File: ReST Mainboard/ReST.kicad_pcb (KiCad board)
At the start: 2 copper layers, 100 x 100 mm, 95 parts, among them IC1 AT24C128, P1 CONN_02X08, P10 CONN_01X04, P11 CONN_01X04, P12 CONN_02X04, P13 CONN_01X03, P14 CONN_02X03, P15 CONN_01X05, P16 CONN_01X03, P17 CONN_01X04, P18 CONN_02X04, P19 CONN_01X04, P2 CONN_02X08, P20 CONN_02X04, P21 CONN_02X04, P22 CONN_01X03, P23 CONN_01X06, P24 CONN_01X03, P25 CONN_01X06, P26 CONN_01X03, P27 CONN_01X06, P28 CONN_01X03, P3 CONN_02X07, P30 CONN_01X03, P32 CONN_01X03, P34 CONN_01X03, P35 SCREW_01X04, P36 SCREW_01X04, P37 SCREW_01X04, P38 SCREW_01X04, P39 CONN_02X04, P4 CONN_02X10, P40 CONN_01X04, P41 CONN_01X04, P42 CONN_01X04, P43 CONN_02X03, P44 CONN_02X03, P45 CONN_02X03, P46 CONN_02X03, P5 USB_OTG, P6 CONN_02X05, P7 CONN_02X05, P8 CONN_01X09, P9 CONN_01X02, SW1 SW-SPST-NO, U1 STM32F103VE, U2 USBLC6-2, U3 L7805ACD2T-TR, U4 LM2574N-ADJ, U5 POLOLU_A4988, U6 POLOLU_A4988, U7 POLOLU_A4988, U8 POLOLU_A4988, X1 Crystal_Small

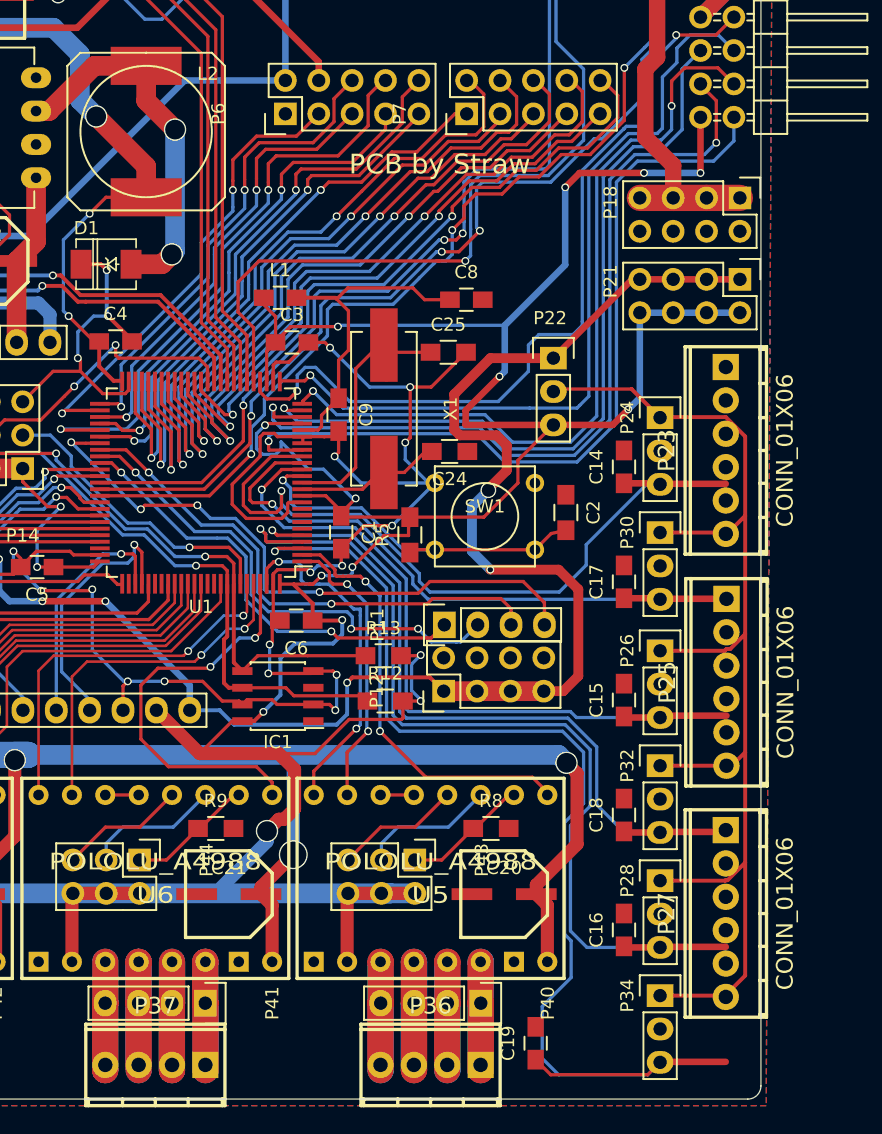
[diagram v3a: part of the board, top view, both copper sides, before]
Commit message: Added relative paths and linked footprint to a extra repo
hope i finally fixed the problem with missing libs. will try to add the
3d views, too
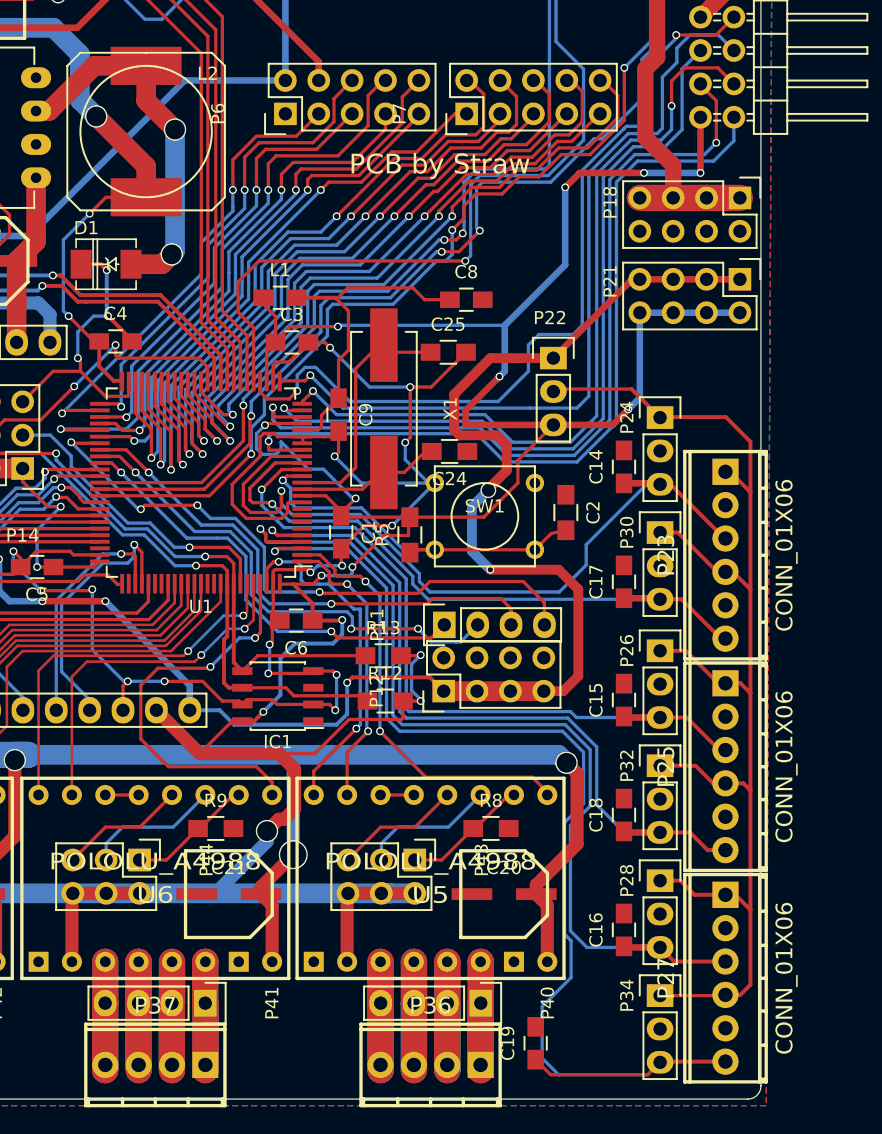
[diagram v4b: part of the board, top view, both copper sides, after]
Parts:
- moved P23 7.98 mm to (196.8, 114.0)
- moved P25 6.43 mm to (196.8, 130.2)
- moved P27 4.93 mm to (196.8, 146.2)
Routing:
- net /ENDSTOP_VCC: track 38.9 -> 100.1 mm
- net /X-MAX: track 78.5 -> 49.5 mm
- net /Y-MAX: track 78.7 -> 58.2 mm
- net /Z-MAX: track 90.8 -> 88.7 mm
- net /X-MIN: track 56.6 -> 58.4 mm
- net /Y-MIN: track 55.7 -> 56.8 mm

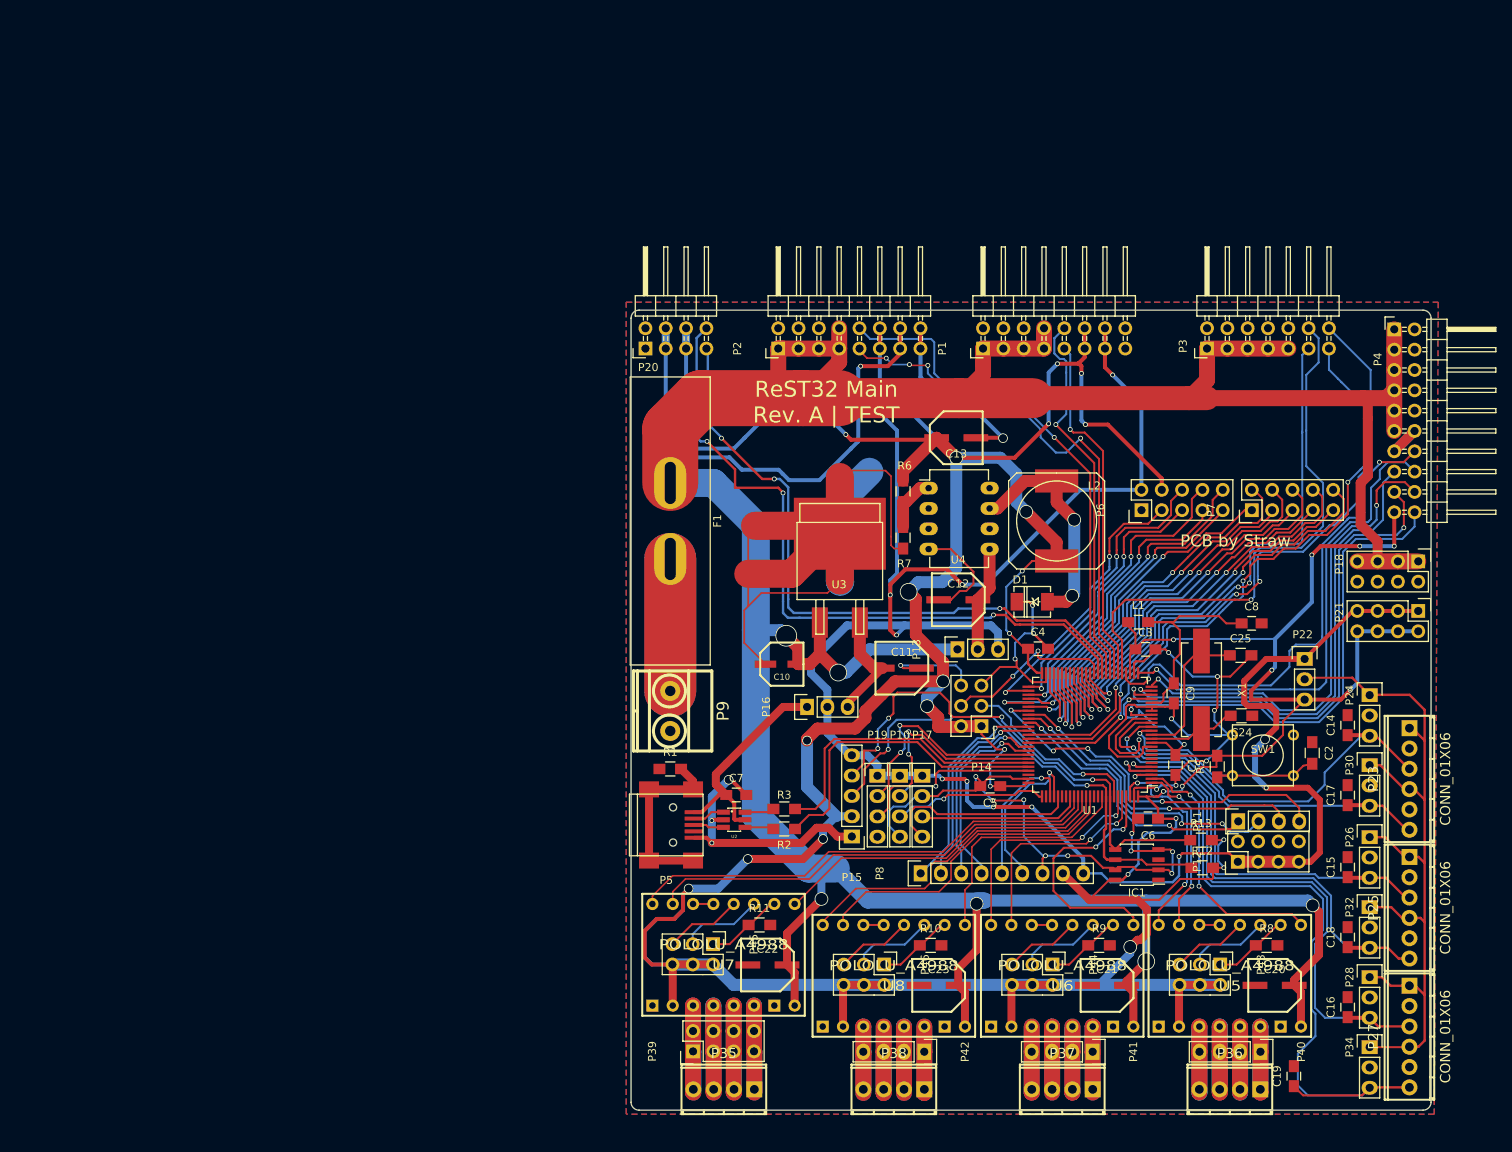
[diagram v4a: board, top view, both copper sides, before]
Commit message: Finished PCB design, notations and silkscreen
gonna work to finish a combined design for cheaper pcb cost and put
everything i need into the bom
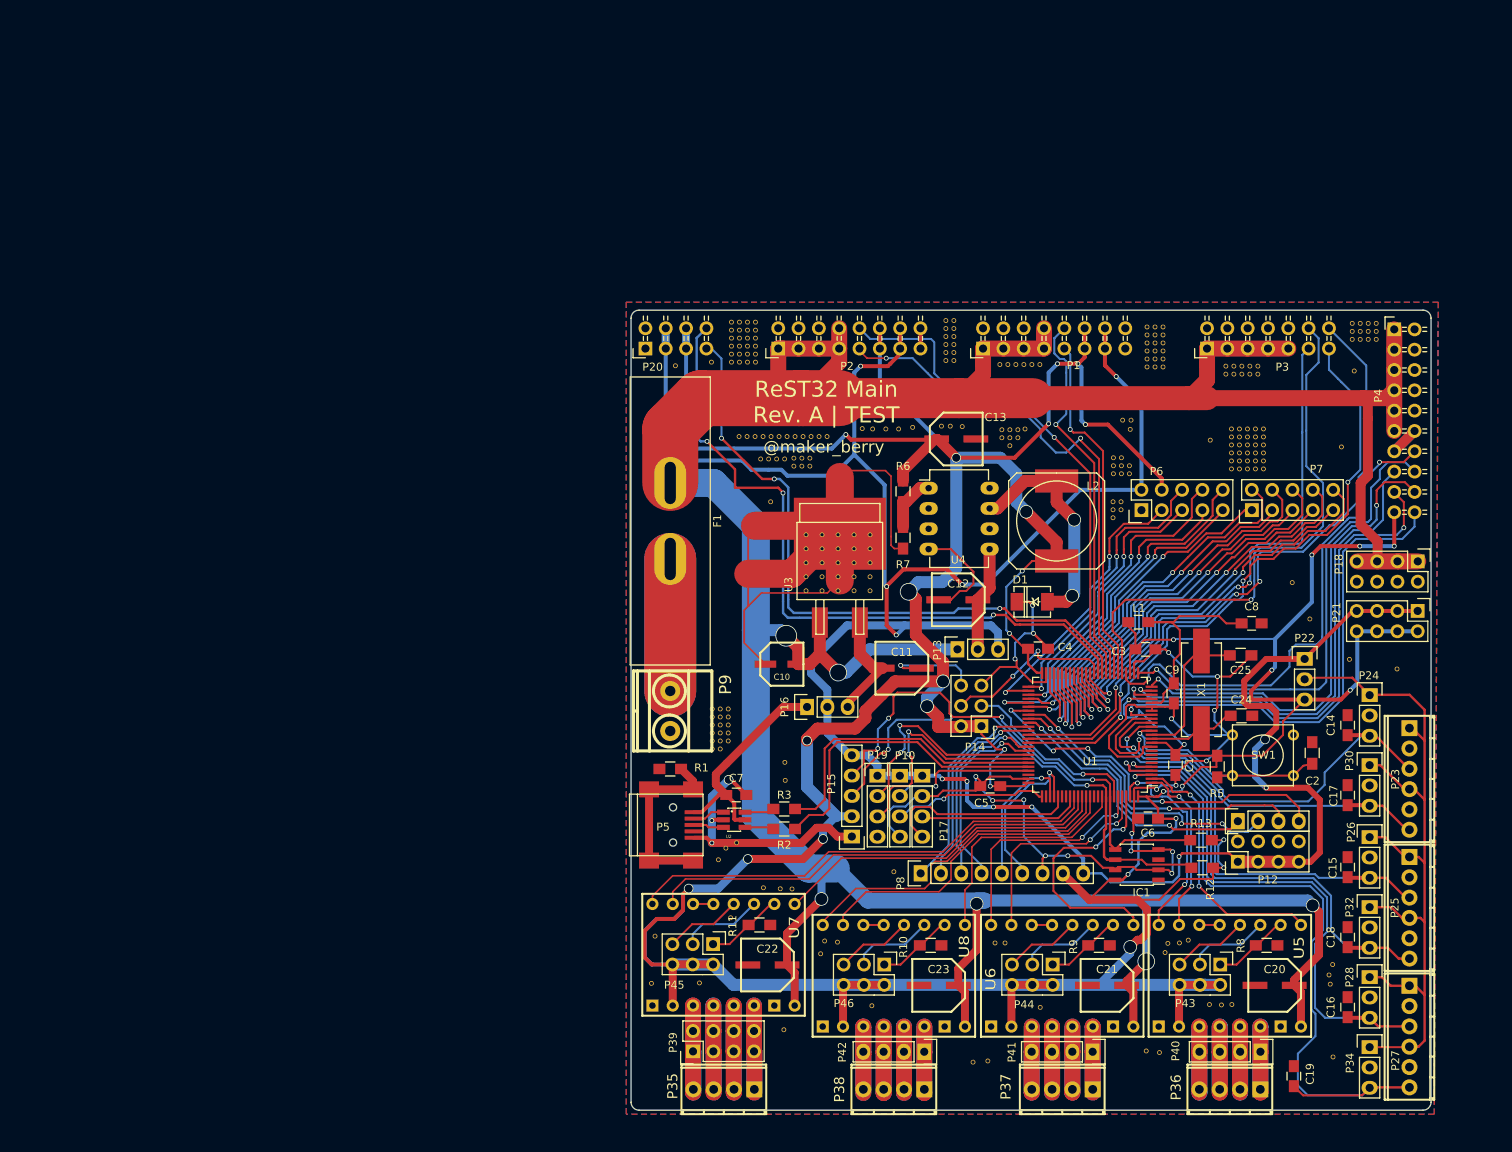
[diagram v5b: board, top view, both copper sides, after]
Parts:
- added REF**11: VIA-0.6mm, ReST-Library:VIA-0.6mm, F.Cu at (119.8, 74.0)
- added REF**111: VIA-0.6mm, ReST-Library:VIA-0.6mm, F.Cu at (115.7, 74.0)
- added REF**111: VIA-0.6mm, ReST-Library:VIA-0.6mm, F.Cu at (109.6, 105.3)
- added REF**111: VIA-0.6mm, ReST-Library:VIA-0.6mm, F.Cu at (112.0, 57.0)
- added REF**11101: VIA-0.6mm, ReST-Library:VIA-0.6mm, F.Cu at (122.0, 71.2)
- added REF**1111: VIA-0.6mm, ReST-Library:VIA-0.6mm, F.Cu at (113.0, 71.2)
- added REF**1111: VIA-0.6mm, ReST-Library:VIA-0.6mm, F.Cu at (163.9, 57.5)
- added REF**11111: VIA-0.6mm, ReST-Library:VIA-0.6mm, F.Cu at (123.0, 71.2)
- added REF**11111: VIA-0.6mm, ReST-Library:VIA-0.6mm, F.Cu at (138.8, 56.8)
- added REF**111111: VIA-0.6mm, ReST-Library:VIA-0.6mm, F.Cu at (174.5, 70.3)
- added REF**111112: VIA-0.6mm, ReST-Library:VIA-0.6mm, F.Cu at (174.5, 71.3)
- added REF**111113: VIA-0.6mm, ReST-Library:VIA-0.6mm, F.Cu at (174.5, 72.3)
- added REF**111114: VIA-0.6mm, ReST-Library:VIA-0.6mm, F.Cu at (174.5, 73.3)
- added REF**111115: VIA-0.6mm, ReST-Library:VIA-0.6mm, F.Cu at (174.5, 74.3)
- added REF**111116: VIA-0.6mm, ReST-Library:VIA-0.6mm, F.Cu at (174.5, 75.3)
- added REF**11112: VIA-0.6mm, ReST-Library:VIA-0.6mm, F.Cu at (138.8, 57.8)
- added REF**111121: VIA-0.6mm, ReST-Library:VIA-0.6mm, F.Cu at (175.5, 70.3)
- added REF**111122: VIA-0.6mm, ReST-Library:VIA-0.6mm, F.Cu at (175.5, 71.3)
- added REF**111123: VIA-0.6mm, ReST-Library:VIA-0.6mm, F.Cu at (175.5, 72.3)
- added REF**111124: VIA-0.6mm, ReST-Library:VIA-0.6mm, F.Cu at (175.5, 73.3)
- added REF**111125: VIA-0.6mm, ReST-Library:VIA-0.6mm, F.Cu at (175.5, 74.3)
- added REF**111126: VIA-0.6mm, ReST-Library:VIA-0.6mm, F.Cu at (175.5, 75.3)
- added REF**11113: VIA-0.6mm, ReST-Library:VIA-0.6mm, F.Cu at (138.8, 58.8)
- added REF**111131: VIA-0.6mm, ReST-Library:VIA-0.6mm, F.Cu at (176.5, 70.3)
- added REF**111132: VIA-0.6mm, ReST-Library:VIA-0.6mm, F.Cu at (176.5, 71.3)
- added REF**111133: VIA-0.6mm, ReST-Library:VIA-0.6mm, F.Cu at (176.5, 72.3)
- added REF**111134: VIA-0.6mm, ReST-Library:VIA-0.6mm, F.Cu at (176.5, 73.3)
- added REF**111135: VIA-0.6mm, ReST-Library:VIA-0.6mm, F.Cu at (176.5, 74.3)
- added REF**111136: VIA-0.6mm, ReST-Library:VIA-0.6mm, F.Cu at (176.5, 75.3)
- added REF**11114: VIA-0.6mm, ReST-Library:VIA-0.6mm, F.Cu at (138.8, 59.8)
- added REF**111141: VIA-0.6mm, ReST-Library:VIA-0.6mm, F.Cu at (177.5, 70.3)
- added REF**111142: VIA-0.6mm, ReST-Library:VIA-0.6mm, F.Cu at (177.5, 71.3)
- added REF**111143: VIA-0.6mm, ReST-Library:VIA-0.6mm, F.Cu at (177.5, 72.3)
- added REF**111144: VIA-0.6mm, ReST-Library:VIA-0.6mm, F.Cu at (177.5, 73.3)
- added REF**111145: VIA-0.6mm, ReST-Library:VIA-0.6mm, F.Cu at (177.5, 74.3)
- added REF**111146: VIA-0.6mm, ReST-Library:VIA-0.6mm, F.Cu at (177.5, 75.3)
- added REF**11115: VIA-0.6mm, ReST-Library:VIA-0.6mm, F.Cu at (138.8, 60.8)
- added REF**111151: VIA-0.6mm, ReST-Library:VIA-0.6mm, F.Cu at (178.5, 70.3)
- added REF**111152: VIA-0.6mm, ReST-Library:VIA-0.6mm, F.Cu at (178.5, 71.3)
- added REF**111153: VIA-0.6mm, ReST-Library:VIA-0.6mm, F.Cu at (178.5, 72.3)
- added REF**111154: VIA-0.6mm, ReST-Library:VIA-0.6mm, F.Cu at (178.5, 73.3)
- added REF**111155: VIA-0.6mm, ReST-Library:VIA-0.6mm, F.Cu at (178.5, 74.3)
- added REF**111156: VIA-0.6mm, ReST-Library:VIA-0.6mm, F.Cu at (178.5, 75.3)
- added REF**11116: VIA-0.6mm, ReST-Library:VIA-0.6mm, F.Cu at (138.8, 61.8)
- added REF**1112: VIA-0.6mm, ReST-Library:VIA-0.6mm, F.Cu at (163.9, 58.5)
- added REF**11121: VIA-0.6mm, ReST-Library:VIA-0.6mm, F.Cu at (124.0, 71.2)
- added REF**11121: VIA-0.6mm, ReST-Library:VIA-0.6mm, F.Cu at (139.8, 56.8)
- added REF**11122: VIA-0.6mm, ReST-Library:VIA-0.6mm, F.Cu at (139.8, 57.8)
- added REF**11123: VIA-0.6mm, ReST-Library:VIA-0.6mm, F.Cu at (139.8, 58.8)
- added REF**11124: VIA-0.6mm, ReST-Library:VIA-0.6mm, F.Cu at (139.8, 59.8)
- added REF**11125: VIA-0.6mm, ReST-Library:VIA-0.6mm, F.Cu at (139.8, 60.8)
- added REF**11126: VIA-0.6mm, ReST-Library:VIA-0.6mm, F.Cu at (139.8, 61.8)
- added REF**1113: VIA-0.6mm, ReST-Library:VIA-0.6mm, F.Cu at (163.9, 59.5)
- added REF**1114: VIA-0.6mm, ReST-Library:VIA-0.6mm, F.Cu at (163.9, 60.5)
- added REF**1115: VIA-0.6mm, ReST-Library:VIA-0.6mm, F.Cu at (163.9, 61.5)
- added REF**1116: VIA-0.6mm, ReST-Library:VIA-0.6mm, F.Cu at (163.9, 62.5)
- added REF**112: VIA-0.6mm, ReST-Library:VIA-0.6mm, F.Cu at (109.6, 106.3)
- added REF**112: VIA-0.6mm, ReST-Library:VIA-0.6mm, F.Cu at (112.0, 58.0)
- added REF**1121: VIA-0.6mm, ReST-Library:VIA-0.6mm, F.Cu at (114.0, 71.2)
- added REF**1121: VIA-0.6mm, ReST-Library:VIA-0.6mm, F.Cu at (164.9, 57.5)
- added REF**1122: VIA-0.6mm, ReST-Library:VIA-0.6mm, F.Cu at (164.9, 58.5)
- added REF**1123: VIA-0.6mm, ReST-Library:VIA-0.6mm, F.Cu at (164.9, 59.5)
- added REF**1124: VIA-0.6mm, ReST-Library:VIA-0.6mm, F.Cu at (164.9, 60.5)
- added REF**1125: VIA-0.6mm, ReST-Library:VIA-0.6mm, F.Cu at (164.9, 61.5)
- added REF**1126: VIA-0.6mm, ReST-Library:VIA-0.6mm, F.Cu at (164.9, 62.5)
- added REF**113: VIA-0.6mm, ReST-Library:VIA-0.6mm, F.Cu at (109.6, 107.3)
- added REF**113: VIA-0.6mm, ReST-Library:VIA-0.6mm, F.Cu at (112.0, 59.0)
- added REF**1131: VIA-0.6mm, ReST-Library:VIA-0.6mm, F.Cu at (115.0, 71.2)
- added REF**1131: VIA-0.6mm, ReST-Library:VIA-0.6mm, F.Cu at (165.9, 57.5)
- added REF**1132: VIA-0.6mm, ReST-Library:VIA-0.6mm, F.Cu at (165.9, 58.5)
- added REF**1133: VIA-0.6mm, ReST-Library:VIA-0.6mm, F.Cu at (165.9, 59.5)
- added REF**1134: VIA-0.6mm, ReST-Library:VIA-0.6mm, F.Cu at (165.9, 60.5)
- added REF**1135: VIA-0.6mm, ReST-Library:VIA-0.6mm, F.Cu at (165.9, 61.5)
- added REF**1136: VIA-0.6mm, ReST-Library:VIA-0.6mm, F.Cu at (165.9, 62.5)
- added REF**114: VIA-0.6mm, ReST-Library:VIA-0.6mm, F.Cu at (109.6, 108.3)
- added REF**114: VIA-0.6mm, ReST-Library:VIA-0.6mm, F.Cu at (112.0, 60.0)
- added REF**1141: VIA-0.6mm, ReST-Library:VIA-0.6mm, F.Cu at (116.0, 71.2)
- added REF**115: VIA-0.6mm, ReST-Library:VIA-0.6mm, F.Cu at (109.6, 109.3)
- added REF**115: VIA-0.6mm, ReST-Library:VIA-0.6mm, F.Cu at (112.0, 61.0)
- added REF**1151: VIA-0.6mm, ReST-Library:VIA-0.6mm, F.Cu at (117.0, 71.2)
- added REF**116: VIA-0.6mm, ReST-Library:VIA-0.6mm, F.Cu at (109.6, 110.3)
- added REF**116: VIA-0.6mm, ReST-Library:VIA-0.6mm, F.Cu at (112.0, 62.0)
- added REF**1161: VIA-0.6mm, ReST-Library:VIA-0.6mm, F.Cu at (118.0, 71.2)
- added REF**1171: VIA-0.6mm, ReST-Library:VIA-0.6mm, F.Cu at (119.0, 71.2)
- added REF**1181: VIA-0.6mm, ReST-Library:VIA-0.6mm, F.Cu at (120.0, 71.2)
- added REF**1191: VIA-0.6mm, ReST-Library:VIA-0.6mm, F.Cu at (121.0, 71.2)
- added REF**12: VIA-0.6mm, ReST-Library:VIA-0.6mm, F.Cu at (119.8, 75.0)
- added REF**121: VIA-0.6mm, ReST-Library:VIA-0.6mm, F.Cu at (116.7, 74.0)
- added REF**121: VIA-0.6mm, ReST-Library:VIA-0.6mm, F.Cu at (110.6, 105.3)
- added REF**121: VIA-0.6mm, ReST-Library:VIA-0.6mm, F.Cu at (113.0, 57.0)
- added REF**122: VIA-0.6mm, ReST-Library:VIA-0.6mm, F.Cu at (110.6, 106.3)
- added REF**122: VIA-0.6mm, ReST-Library:VIA-0.6mm, F.Cu at (113.0, 58.0)
- added REF**123: VIA-0.6mm, ReST-Library:VIA-0.6mm, F.Cu at (110.6, 107.3)
- added REF**123: VIA-0.6mm, ReST-Library:VIA-0.6mm, F.Cu at (113.0, 59.0)
- added REF**124: VIA-0.6mm, ReST-Library:VIA-0.6mm, F.Cu at (110.6, 108.3)
- added REF**124: VIA-0.6mm, ReST-Library:VIA-0.6mm, F.Cu at (113.0, 60.0)
- added REF**125: VIA-0.6mm, ReST-Library:VIA-0.6mm, F.Cu at (110.6, 109.3)
- added REF**125: VIA-0.6mm, ReST-Library:VIA-0.6mm, F.Cu at (113.0, 61.0)
- added REF**126: VIA-0.6mm, ReST-Library:VIA-0.6mm, F.Cu at (110.6, 110.3)
- added REF**126: VIA-0.6mm, ReST-Library:VIA-0.6mm, F.Cu at (113.0, 62.0)
- added REF**131: VIA-0.6mm, ReST-Library:VIA-0.6mm, F.Cu at (118.7, 114.2)
- added REF**131: VIA-0.6mm, ReST-Library:VIA-0.6mm, F.Cu at (118.7, 112.0)
- added REF**131: VIA-0.6mm, ReST-Library:VIA-0.6mm, F.Cu at (117.7, 74.0)
- added REF**131: VIA-0.6mm, ReST-Library:VIA-0.6mm, F.Cu at (111.6, 105.3)
- added REF**131: VIA-0.6mm, ReST-Library:VIA-0.6mm, F.Cu at (114.0, 57.0)
- added REF**131111: VIA-0.6mm, ReST-Library:VIA-0.6mm, F.Cu at (121.3, 83.5)
- added REF**131112: VIA-0.6mm, ReST-Library:VIA-0.6mm, F.Cu at (121.3, 85.3)
- added REF**131113: VIA-0.6mm, ReST-Library:VIA-0.6mm, F.Cu at (121.3, 87.0)
- added REF**131114: VIA-0.6mm, ReST-Library:VIA-0.6mm, F.Cu at (121.3, 88.8)
- added REF**131115: VIA-0.6mm, ReST-Library:VIA-0.6mm, F.Cu at (121.3, 90.5)
- added REF**131121: VIA-0.6mm, ReST-Library:VIA-0.6mm, F.Cu at (123.3, 83.5)
- added REF**131122: VIA-0.6mm, ReST-Library:VIA-0.6mm, F.Cu at (123.3, 85.3)
- added REF**131123: VIA-0.6mm, ReST-Library:VIA-0.6mm, F.Cu at (123.3, 87.0)
- added REF**131124: VIA-0.6mm, ReST-Library:VIA-0.6mm, F.Cu at (123.3, 88.8)
- added REF**131125: VIA-0.6mm, ReST-Library:VIA-0.6mm, F.Cu at (123.3, 90.5)
- added REF**131131: VIA-0.6mm, ReST-Library:VIA-0.6mm, F.Cu at (125.3, 83.5)
- added REF**131132: VIA-0.6mm, ReST-Library:VIA-0.6mm, F.Cu at (125.3, 85.3)
- added REF**131133: VIA-0.6mm, ReST-Library:VIA-0.6mm, F.Cu at (125.3, 87.0)
- added REF**131134: VIA-0.6mm, ReST-Library:VIA-0.6mm, F.Cu at (125.3, 88.8)
- added REF**131135: VIA-0.6mm, ReST-Library:VIA-0.6mm, F.Cu at (125.3, 90.5)
- added REF**131141: VIA-0.6mm, ReST-Library:VIA-0.6mm, F.Cu at (127.3, 83.5)
- added REF**131142: VIA-0.6mm, ReST-Library:VIA-0.6mm, F.Cu at (127.3, 85.3)
- added REF**131143: VIA-0.6mm, ReST-Library:VIA-0.6mm, F.Cu at (127.3, 87.0)
- added REF**131144: VIA-0.6mm, ReST-Library:VIA-0.6mm, F.Cu at (127.3, 88.8)
- added REF**131145: VIA-0.6mm, ReST-Library:VIA-0.6mm, F.Cu at (127.3, 90.5)
- added REF**131151: VIA-0.6mm, ReST-Library:VIA-0.6mm, F.Cu at (129.3, 83.5)
- added REF**131152: VIA-0.6mm, ReST-Library:VIA-0.6mm, F.Cu at (129.3, 85.3)
- added REF**131153: VIA-0.6mm, ReST-Library:VIA-0.6mm, F.Cu at (129.3, 87.0)
- added REF**131154: VIA-0.6mm, ReST-Library:VIA-0.6mm, F.Cu at (129.3, 88.8)
- added REF**131155: VIA-0.6mm, ReST-Library:VIA-0.6mm, F.Cu at (129.3, 90.5)
- added REF**132: VIA-0.6mm, ReST-Library:VIA-0.6mm, F.Cu at (111.6, 106.3)
- added REF**132: VIA-0.6mm, ReST-Library:VIA-0.6mm, F.Cu at (114.0, 58.0)
- added REF**133: VIA-0.6mm, ReST-Library:VIA-0.6mm, F.Cu at (111.6, 107.3)
- added REF**133: VIA-0.6mm, ReST-Library:VIA-0.6mm, F.Cu at (114.0, 59.0)
- added REF**134: VIA-0.6mm, ReST-Library:VIA-0.6mm, F.Cu at (111.6, 108.3)
- added REF**134: VIA-0.6mm, ReST-Library:VIA-0.6mm, F.Cu at (114.0, 60.0)
- added REF**135: VIA-0.6mm, ReST-Library:VIA-0.6mm, F.Cu at (111.6, 109.3)
- added REF**135: VIA-0.6mm, ReST-Library:VIA-0.6mm, F.Cu at (114.0, 61.0)
- added REF**136: VIA-0.6mm, ReST-Library:VIA-0.6mm, F.Cu at (114.0, 62.0)
- added REF**141: VIA-0.6mm, ReST-Library:VIA-0.6mm, F.Cu at (118.7, 74.0)
- added REF**141: VIA-0.6mm, ReST-Library:VIA-0.6mm, F.Cu at (115.0, 57.0)
- added REF**142: VIA-0.6mm, ReST-Library:VIA-0.6mm, F.Cu at (115.0, 58.0)
- added REF**143: VIA-0.6mm, ReST-Library:VIA-0.6mm, F.Cu at (115.0, 59.0)
- added REF**144: VIA-0.6mm, ReST-Library:VIA-0.6mm, F.Cu at (115.0, 60.0)
- added REF**145: VIA-0.6mm, ReST-Library:VIA-0.6mm, F.Cu at (115.0, 61.0)
- added REF**146: VIA-0.6mm, ReST-Library:VIA-0.6mm, F.Cu at (115.0, 62.0)
- added REF**21: VIA-0.6mm, ReST-Library:VIA-0.6mm, F.Cu at (120.8, 74.0)
- added REF**22: VIA-0.6mm, ReST-Library:VIA-0.6mm, F.Cu at (120.8, 75.0)
- added REF**31: VIA-0.6mm, ReST-Library:VIA-0.6mm, F.Cu at (110.4, 124.2)
- added REF**31: VIA-0.6mm, ReST-Library:VIA-0.6mm, F.Cu at (142.2, 149.4)
- added REF**31: VIA-0.6mm, ReST-Library:VIA-0.6mm, F.Cu at (129.6, 142.4)
- added REF**31: VIA-0.6mm, ReST-Library:VIA-0.6mm, F.Cu at (123.2, 135.9)
- added REF**31: VIA-0.6mm, ReST-Library:VIA-0.6mm, F.Cu at (125.2, 134.4)
- added REF**31: VIA-0.6mm, ReST-Library:VIA-0.6mm, F.Cu at (123.7, 134.3)
- added REF**31: VIA-0.6mm, ReST-Library:VIA-0.6mm, F.Cu at (146.2, 134.6)
- added REF**31: VIA-0.6mm, ReST-Library:VIA-0.6mm, F.Cu at (144.9, 134.6)
- added REF**31: VIA-0.6mm, ReST-Library:VIA-0.6mm, F.Cu at (150.6, 142.6)
- added REF**31: VIA-0.6mm, ReST-Library:VIA-0.6mm, F.Cu at (165.5, 148.2)
- added REF**31: VIA-0.6mm, ReST-Library:VIA-0.6mm, F.Cu at (163.8, 148.1)
- added REF**31: VIA-0.6mm, ReST-Library:VIA-0.6mm, F.Cu at (112.7, 122.0)
- added REF**31: VIA-0.6mm, ReST-Library:VIA-0.6mm, F.Cu at (187.2, 148.8)
- added REF**31: VIA-0.6mm, ReST-Library:VIA-0.6mm, F.Cu at (186.8, 139.7)
- added REF**31: VIA-0.6mm, ReST-Library:VIA-0.6mm, F.Cu at (186.7, 138.6)
- added REF**31: VIA-0.6mm, ReST-Library:VIA-0.6mm, F.Cu at (187.2, 137.2)
- added REF**31: VIA-0.6mm, ReST-Library:VIA-0.6mm, F.Cu at (174.6, 142.2)
- added REF**31: VIA-0.6mm, ReST-Library:VIA-0.6mm, F.Cu at (173.2, 142.3)
- added REF**31: VIA-0.6mm, ReST-Library:VIA-0.6mm, F.Cu at (171.8, 142.2)
- added REF**31: VIA-0.6mm, ReST-Library:VIA-0.6mm, F.Cu at (166.2, 135.8)
- added REF**31: VIA-0.6mm, ReST-Library:VIA-0.6mm, F.Cu at (169.1, 134.2)
- added REF**31: VIA-0.6mm, ReST-Library:VIA-0.6mm, F.Cu at (168.0, 134.6)
- added REF**31: VIA-0.6mm, ReST-Library:VIA-0.6mm, F.Cu at (111.3, 122.7)
- added REF**31: VIA-0.6mm, ReST-Library:VIA-0.6mm, F.Cu at (161.8, 70.3)
- added REF**31: VIA-0.6mm, ReST-Library:VIA-0.6mm, F.Cu at (161.9, 69.2)
- added REF**31: VIA-0.6mm, ReST-Library:VIA-0.6mm, F.Cu at (160.9, 69.2)
- added REF**31: VIA-0.6mm, ReST-Library:VIA-0.6mm, F.Cu at (102.5, 133.7)
- added REF**31: VIA-0.6mm, ReST-Library:VIA-0.6mm, F.Cu at (111.9, 131.4)
- added REF**31: VIA-0.6mm, ReST-Library:VIA-0.6mm, F.Cu at (112.0, 133.3)
- added REF**31: VIA-0.6mm, ReST-Library:VIA-0.6mm, F.Cu at (116.0, 127.7)
- added REF**31: VIA-0.6mm, ReST-Library:VIA-0.6mm, F.Cu at (132.3, 125.7)
- added REF**31: VIA-0.6mm, ReST-Library:VIA-0.6mm, F.Cu at (166.6, 134.6)
- added REF**31: VIA-0.6mm, ReST-Library:VIA-0.6mm, F.Cu at (189.2, 99.1)
- added REF**31: VIA-0.6mm, ReST-Library:VIA-0.6mm, F.Cu at (119.6, 127.8)
- added REF**31: VIA-0.6mm, ReST-Library:VIA-0.6mm, F.Cu at (195.2, 100.3)
- added REF**31: VIA-0.6mm, ReST-Library:VIA-0.6mm, F.Cu at (184.3, 94.0)
- added REF**31: VIA-0.6mm, ReST-Library:VIA-0.6mm, F.Cu at (182.1, 89.5)
- added REF**31: VIA-0.6mm, ReST-Library:VIA-0.6mm, F.Cu at (189.8, 63.0)
- added REF**31: VIA-0.6mm, ReST-Library:VIA-0.6mm, F.Cu at (188.2, 72.5)
- added REF**31: VIA-0.6mm, ReST-Library:VIA-0.6mm, F.Cu at (171.8, 71.7)
- added REF**31: VIA-0.6mm, ReST-Library:VIA-0.6mm, F.Cu at (109.5, 62.0)
- added REF**31: VIA-0.6mm, ReST-Library:VIA-0.6mm, F.Cu at (105.0, 62.4)
- added REF**31: VIA-0.6mm, ReST-Library:VIA-0.6mm, F.Cu at (116.9, 79.4)
- added REF**31: VIA-0.6mm, ReST-Library:VIA-0.6mm, F.Cu at (121.8, 74.0)
- added REF**31: VIA-0.6mm, ReST-Library:VIA-0.6mm, F.Cu at (118.1, 127.8)
- added REF**31: VIA-0.6mm, ReST-Library:VIA-0.6mm, F.Cu at (102.0, 139.6)
- added REF**31: VIA-0.6mm, ReST-Library:VIA-0.6mm, F.Cu at (108.0, 139.6)
- added REF**31: VIA-0.6mm, ReST-Library:VIA-0.6mm, F.Cu at (118.5, 145.4)
- added REF**31: VIA-0.6mm, ReST-Library:VIA-0.6mm, F.Cu at (144.1, 149.3)
- added REF**311: VIA-0.6mm, ReST-Library:VIA-0.6mm, F.Cu at (145.8, 70.4)
- added REF**311: VIA-0.6mm, ReST-Library:VIA-0.6mm, F.Cu at (189.6, 57.1)
- added REF**311: VIA-0.6mm, ReST-Library:VIA-0.6mm, F.Cu at (159.8, 73.9)
- added REF**3111: VIA-0.6mm, ReST-Library:VIA-0.6mm, F.Cu at (173.8, 62.5)
- added REF**3111: VIA-0.6mm, ReST-Library:VIA-0.6mm, F.Cu at (159.7, 79.4)
- added REF**3111: VIA-0.6mm, ReST-Library:VIA-0.6mm, F.Cu at (145.6, 62.2)
- added REF**3112: VIA-0.6mm, ReST-Library:VIA-0.6mm, F.Cu at (173.8, 63.5)
- added REF**3112: VIA-0.6mm, ReST-Library:VIA-0.6mm, F.Cu at (159.7, 80.4)
- added REF**3113: VIA-0.6mm, ReST-Library:VIA-0.6mm, F.Cu at (159.7, 81.4)
- added REF**312: VIA-0.6mm, ReST-Library:VIA-0.6mm, F.Cu at (145.8, 71.4)
- added REF**312: VIA-0.6mm, ReST-Library:VIA-0.6mm, F.Cu at (189.6, 58.1)
- added REF**312: VIA-0.6mm, ReST-Library:VIA-0.6mm, F.Cu at (159.8, 74.9)
- added REF**3121: VIA-0.6mm, ReST-Library:VIA-0.6mm, F.Cu at (174.8, 62.5)
- added REF**3121: VIA-0.6mm, ReST-Library:VIA-0.6mm, F.Cu at (160.7, 79.4)
- added REF**3121: VIA-0.6mm, ReST-Library:VIA-0.6mm, F.Cu at (146.6, 62.2)
- added REF**3122: VIA-0.6mm, ReST-Library:VIA-0.6mm, F.Cu at (174.8, 63.5)
- added REF**3122: VIA-0.6mm, ReST-Library:VIA-0.6mm, F.Cu at (160.7, 80.4)
- added REF**313: VIA-0.6mm, ReST-Library:VIA-0.6mm, F.Cu at (128.3, 70.2)
- added REF**313: VIA-0.6mm, ReST-Library:VIA-0.6mm, F.Cu at (159.8, 75.9)
- added REF**313: VIA-0.6mm, ReST-Library:VIA-0.6mm, F.Cu at (129.7, 70.3)
- added REF**313: VIA-0.6mm, ReST-Library:VIA-0.6mm, F.Cu at (131.3, 70.3)
- added REF**313: VIA-0.6mm, ReST-Library:VIA-0.6mm, F.Cu at (132.9, 70.3)
- added REF**313: VIA-0.6mm, ReST-Library:VIA-0.6mm, F.Cu at (134.7, 70.1)
- added REF**313: VIA-0.6mm, ReST-Library:VIA-0.6mm, F.Cu at (138.2, 70.0)
- added REF**313: VIA-0.6mm, ReST-Library:VIA-0.6mm, F.Cu at (139.3, 70.0)
- added REF**313: VIA-0.6mm, ReST-Library:VIA-0.6mm, F.Cu at (140.8, 70.0)
- added REF**313: VIA-0.6mm, ReST-Library:VIA-0.6mm, F.Cu at (189.6, 59.1)
- added REF**3131: VIA-0.6mm, ReST-Library:VIA-0.6mm, F.Cu at (175.8, 62.5)
- added REF**3131: VIA-0.6mm, ReST-Library:VIA-0.6mm, F.Cu at (147.6, 62.2)
- added REF**3132: VIA-0.6mm, ReST-Library:VIA-0.6mm, F.Cu at (175.8, 63.5)
- added REF**3141: VIA-0.6mm, ReST-Library:VIA-0.6mm, F.Cu at (176.8, 62.5)
- added REF**3141: VIA-0.6mm, ReST-Library:VIA-0.6mm, F.Cu at (148.6, 62.2)
- added REF**3142: VIA-0.6mm, ReST-Library:VIA-0.6mm, F.Cu at (176.8, 63.5)
- added REF**3151: VIA-0.6mm, ReST-Library:VIA-0.6mm, F.Cu at (177.8, 62.5)
- added REF**3151: VIA-0.6mm, ReST-Library:VIA-0.6mm, F.Cu at (149.6, 62.2)
- added REF**3152: VIA-0.6mm, ReST-Library:VIA-0.6mm, F.Cu at (177.8, 63.5)
- added REF**3161: VIA-0.6mm, ReST-Library:VIA-0.6mm, F.Cu at (150.6, 62.2)
- added REF**32: VIA-0.6mm, ReST-Library:VIA-0.6mm, F.Cu at (121.8, 75.0)
- added REF**321: VIA-0.6mm, ReST-Library:VIA-0.6mm, F.Cu at (146.8, 70.4)
- added REF**321: VIA-0.6mm, ReST-Library:VIA-0.6mm, F.Cu at (190.6, 57.1)
- added REF**321: VIA-0.6mm, ReST-Library:VIA-0.6mm, F.Cu at (160.8, 73.9)
- added REF**322: VIA-0.6mm, ReST-Library:VIA-0.6mm, F.Cu at (146.8, 71.4)
- added REF**322: VIA-0.6mm, ReST-Library:VIA-0.6mm, F.Cu at (190.6, 58.1)
- added REF**322: VIA-0.6mm, ReST-Library:VIA-0.6mm, F.Cu at (160.8, 74.9)
- added REF**323: VIA-0.6mm, ReST-Library:VIA-0.6mm, F.Cu at (146.8, 72.4)
- added REF**323: VIA-0.6mm, ReST-Library:VIA-0.6mm, F.Cu at (190.6, 59.1)
- added REF**323: VIA-0.6mm, ReST-Library:VIA-0.6mm, F.Cu at (160.8, 75.9)
- added REF**331: VIA-0.6mm, ReST-Library:VIA-0.6mm, F.Cu at (147.8, 70.4)
- added REF**331: VIA-0.6mm, ReST-Library:VIA-0.6mm, F.Cu at (191.6, 57.1)
- added REF**332: VIA-0.6mm, ReST-Library:VIA-0.6mm, F.Cu at (147.8, 71.4)
- added REF**332: VIA-0.6mm, ReST-Library:VIA-0.6mm, F.Cu at (191.6, 58.1)
- added REF**332: VIA-0.6mm, ReST-Library:VIA-0.6mm, F.Cu at (161.8, 74.9)
- added REF**333: VIA-0.6mm, ReST-Library:VIA-0.6mm, F.Cu at (148.7, 70.3)
- added REF**333: VIA-0.6mm, ReST-Library:VIA-0.6mm, F.Cu at (191.6, 59.1)
- added REF**333: VIA-0.6mm, ReST-Library:VIA-0.6mm, F.Cu at (161.8, 75.9)
- added REF**341: VIA-0.6mm, ReST-Library:VIA-0.6mm, F.Cu at (192.6, 57.1)
- added REF**342: VIA-0.6mm, ReST-Library:VIA-0.6mm, F.Cu at (192.6, 58.1)
- added REF**343: VIA-0.6mm, ReST-Library:VIA-0.6mm, F.Cu at (192.6, 59.1)
- ?: renamed from P11; value CONN_01X04 -> (none)
- C1, C2, C3, C4, C5, C6, C9: value 100nF -> (none)
- C14, C15, C16, C17, C18, C19: value 10nF -> (none)
- C24, C25: value 30pF -> (none)
- C8: value 10uF -> (none)
- IC1: value AT24C128 -> (none)
- L1: value BEAD -> (none)
- P1, P2: value CONN_02X08 -> (none); footprint Pin_Headers:Pin_Header_Angled_2x08 -> ReST-Library:Pin_Header_Angled_2x08
- P10, P17, P19, P40, P41, P42: value CONN_01X04 -> (none)
- P12, P18, P39: value CONN_02X04 -> (none)
- P13, P16, P22: value CONN_01X03 -> (none)
- P14, P43, P44, P45, P46: value CONN_02X03 -> (none)
- P15: value CONN_01X05 -> (none)
- P20: footprint Pin_Headers:Pin_Header_Angled_2x04 -> ReST-Library:Pin_Header_Angled_2x04
- P23, P25, P27: value CONN_01X06 -> (none)
- P3: value CONN_02X07 -> (none); footprint Pin_Headers:Pin_Header_Angled_2x07 -> ReST-Library:Pin_Header_Angled_2x07
- P4: value CONN_02X10 -> (none); footprint Pin_Headers:Pin_Header_Angled_2x10 -> ReST-Library:Pin_Header_Angled_2x10
- P6, P7: value CONN_02X05 -> (none)
- P8: value CONN_01X09 -> (none)
- R10, R11, R8, R9: value 100K -> (none)
- R12, R13: value 4K7 -> (none)
- R5: value 10K -> (none)
- SW1: value SW-SPST-NO -> (none)
- U1: value STM32F103VE -> (none)
- U3: value L7805ACD2T-TR -> (none)
- U5, U6, U7, U8: value POLOLU_A4988 -> (none)
- X1: value Crystal_Small -> (none)
- moved C13 0.15 mm to (140.1, 71.5)
- moved P21 0.07 mm to (197.8, 93.0)
- moved P18 0.06 mm to (197.8, 86.8)
- moved ? 0.05 mm to (175.3, 119.3)
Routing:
- net GND: track 352.7 -> 332.2 mm, vias 24 -> 23
- net (no net): track 15.3 -> 0.00 mm
- net +5V: track 327.7 -> 318.9 mm
- net +3V3: track 652.0 -> 649.9 mm
- net /PWM-ADD1: track 80.2 -> 79.5 mm
- net /PWM-HEAT0: track 66.1 -> 65.6 mm, vias 4 -> 2
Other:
- board text added: "@maker_berry"
- board text removed: "PCB by Straw"

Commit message: Final release
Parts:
- removed the REF**31 at (111.9, 131.4)
- added GND: VIA-0.6mm, ReST-Library:VIA-0.6mm, F.Cu at (27.2, 91.8)
- added REF**131111: VIA-0.6mm, ReST-Library:VIA-0.6mm, F.Cu at (80.8, 101.7)
- added REF**131111: VIA-0.6mm, ReST-Library:VIA-0.6mm, F.Cu at (91.2, 50.8)
- added REF**131111: VIA-0.6mm, ReST-Library:VIA-0.6mm, F.Cu at (76.6, 28.1)
- added REF**131111: VIA-0.6mm, ReST-Library:VIA-0.6mm, F.Cu at (61.6, 60.4)
- added REF**131111: VIA-0.6mm, ReST-Library:VIA-0.6mm, F.Cu at (49.8, 62.1)
- added REF**31: VIA-0.6mm, ReST-Library:VIA-0.6mm, F.Cu at (92.9, 95.1)
- added REF**31: VIA-0.6mm, ReST-Library:VIA-0.6mm, F.Cu at (55.1, 69.4)
- added REF**31: VIA-0.6mm, ReST-Library:VIA-0.6mm, F.Cu at (59.5, 75.5)
- added REF**31: VIA-0.6mm, ReST-Library:VIA-0.6mm, F.Cu at (63.3, 73.9)
- added REF**31: VIA-0.6mm, ReST-Library:VIA-0.6mm, F.Cu at (57.4, 69.3)
- added REF**31: VIA-0.6mm, ReST-Library:VIA-0.6mm, F.Cu at (76.9, 91.8)
- added REF**31: VIA-0.6mm, ReST-Library:VIA-0.6mm, F.Cu at (69.2, 91.8)
- added REF**31: VIA-0.6mm, ReST-Library:VIA-0.6mm, F.Cu at (66.5, 91.7)
- added REF**31: VIA-0.6mm, ReST-Library:VIA-0.6mm, F.Cu at (63.5, 91.6)
- added REF**31: VIA-0.6mm, ReST-Library:VIA-0.6mm, F.Cu at (82.2, 74.5)
- added REF**31: VIA-0.6mm, ReST-Library:VIA-0.6mm, F.Cu at (104.3, 65.3)
- added REF**31: VIA-0.6mm, ReST-Library:VIA-0.6mm, F.Cu at (67.2, 86.7)
- added REF**31: VIA-0.6mm, ReST-Library:VIA-0.6mm, F.Cu at (65.3, 81.5)
- GND: renamed from REF**31; value VIA-0.6mm -> (none)
- moved C9 84.4 mm to (90.8, 67.5)
- moved ? 84.3 mm to (99.0, 83.6)
- moved IC1 84.3 mm to (86.4, 89.0)
- moved P12 84.3 mm to (99.0, 88.6)
- moved P36 84.3 mm to (98.0, 117.1)
- moved P7 84.3 mm to (100.8, 44.7)
- moved REF**31 84.3 mm to (67.8, 113.5)
- moved REF**31 84.3 mm to (98.3, 106.5)
- moved REF**31 84.3 mm to (90.3, 98.8)
- moved REF**31 84.3 mm to (108.0, 58.3)
- moved REF**311 84.3 mm to (69.5, 34.6)
- moved REF**3111 84.3 mm to (97.5, 26.7)
- moved REF**3111 84.3 mm to (69.3, 26.5)
- moved REF**3112 84.3 mm to (97.5, 27.7)
- moved REF**312 84.3 mm to (69.5, 35.6)
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- renumbered REF**31 to GND
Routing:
- net +12V: track 436.1 -> 435.0 mm
- net /Z-DIR: track 59.7 -> 60.6 mm
- net +3V3: track 649.9 -> 649.1 mm
- net +5V: track 318.9 -> 318.0 mm
- net /E2-EN: track 62.8 -> 63.5 mm
